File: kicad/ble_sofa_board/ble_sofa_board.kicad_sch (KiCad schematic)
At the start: 4 parts

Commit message: ble_sofa_board - WIP schematic
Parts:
- added D?: 1N5822, Diode_THT:D_DO-201AD_P15.24mm_Horizontal, symbol Diode:1N5822
- added J?: RJ9, symbol Connector:RJ9
- added SW_RST: SW_Push, symbol Switch:SW_Push
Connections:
- net RELAY2_PIN: now reaches A?.10 (GP7)
- net RELAY2_PIN: now also U?.31 (GP7)
- net GND: now reaches A?.13 (GND)
- net GND: now also A?.18 (GND), A?.23 (GND), A?.28 (GND), A?.3 (GND), A?.33 (AGND), A?.38 (GND), A?.8 (GND), U?.13 (GND), U?.18 (GND), U?.23 (GND), U?.28 (GND), U?.3 (GND), U?.33 (AGND), U?.38 (GND), U?.4 (VOUT-), U?.4 (VOUT-), U?.8 (GND), SW_RST.1
- net at A?.30 (RUN): now also U?.11 (RUN), SW_RST.2
- net at A?.35 (ADC_VREF): now also U?.6 (ADC_VREF)
- net at A?.36 (3V3_OUT): now also U?.5 (3V3_OUT)
- net PICO_3V3EN: now reaches A?.37 (3V3_EN)
- net PICO_3V3EN: now also U?.4 (3V3_EN)
- net at A?.39 (VSYS): now also D?.1 (K)
- net RELAY1_PIN: now reaches A?.9 (GP6)
- net RELAY1_PIN: now also U?.32 (GP6)
- net at U?.1 (VBUS): now also U?.2 (VSYS), U?.3 (VOUT+)
- net VCC: now reaches U?.1 (VIN+)
- net VCC: now also U?.1 (VIN+)
- net GND1: now reaches U?.2 (VIN-)
- net GND1: now also U?.2 (VIN-)
- net at U?.3 (VOUT+): now also D?.2 (A)
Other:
- title: (none) -> BLE Sofa Board
- moved on the sheet: A?, U?

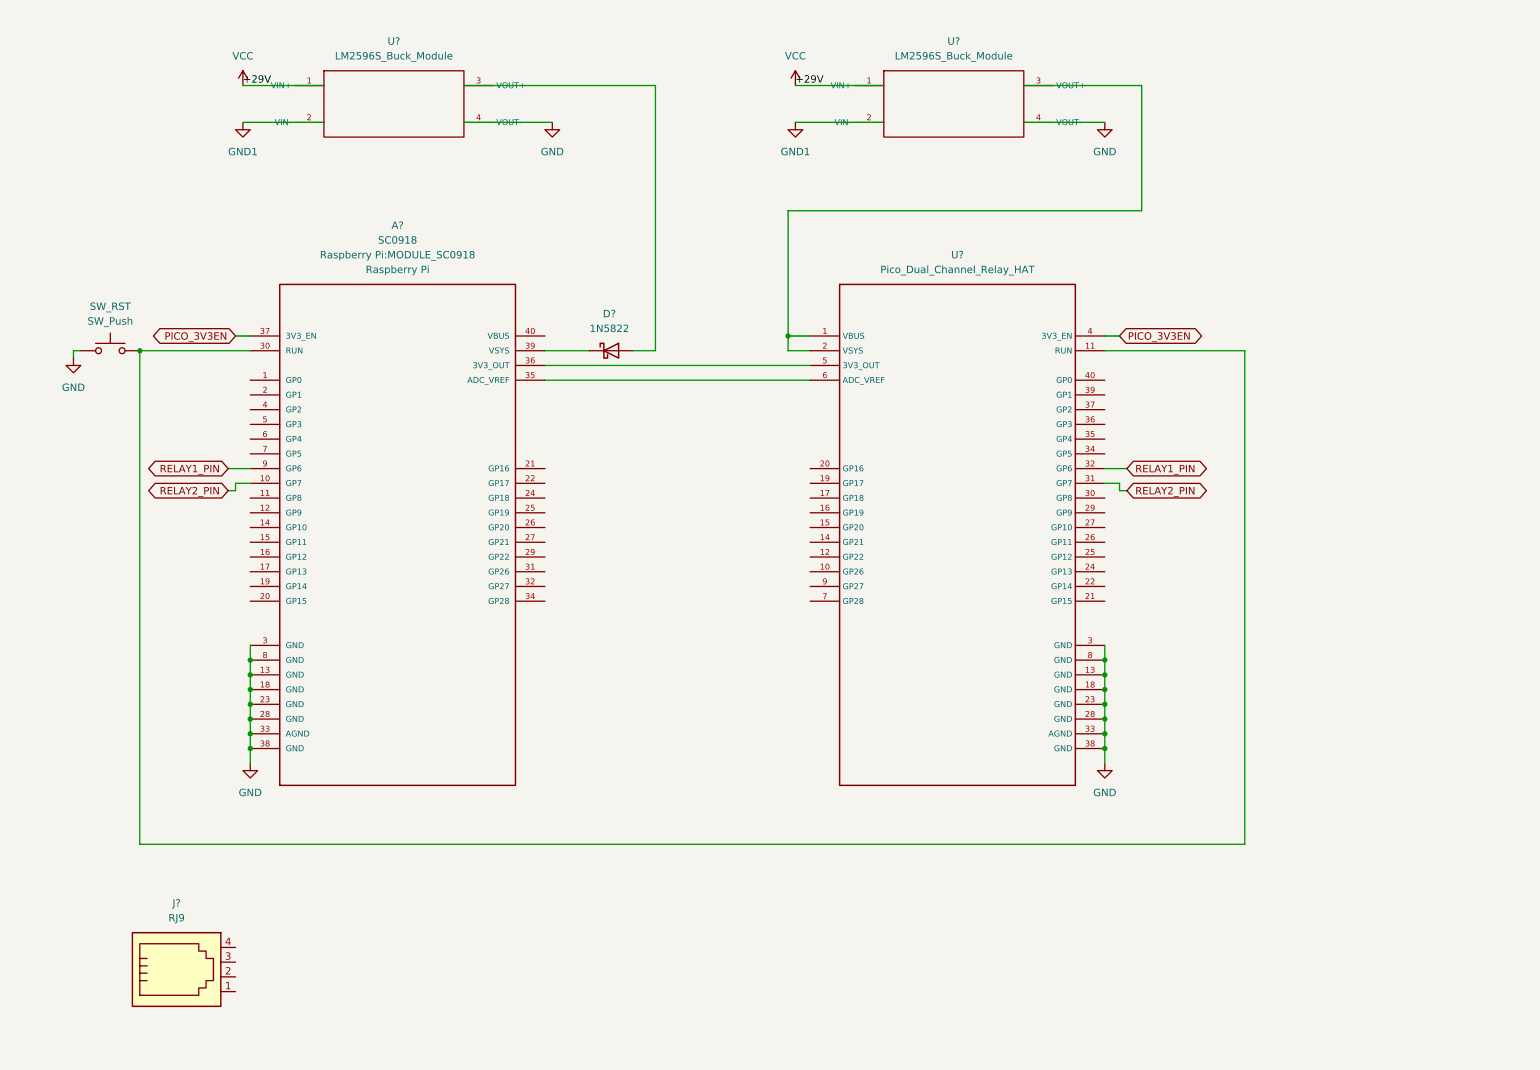
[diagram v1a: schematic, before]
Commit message: ble_sofa_board - Complete schematic and PCB
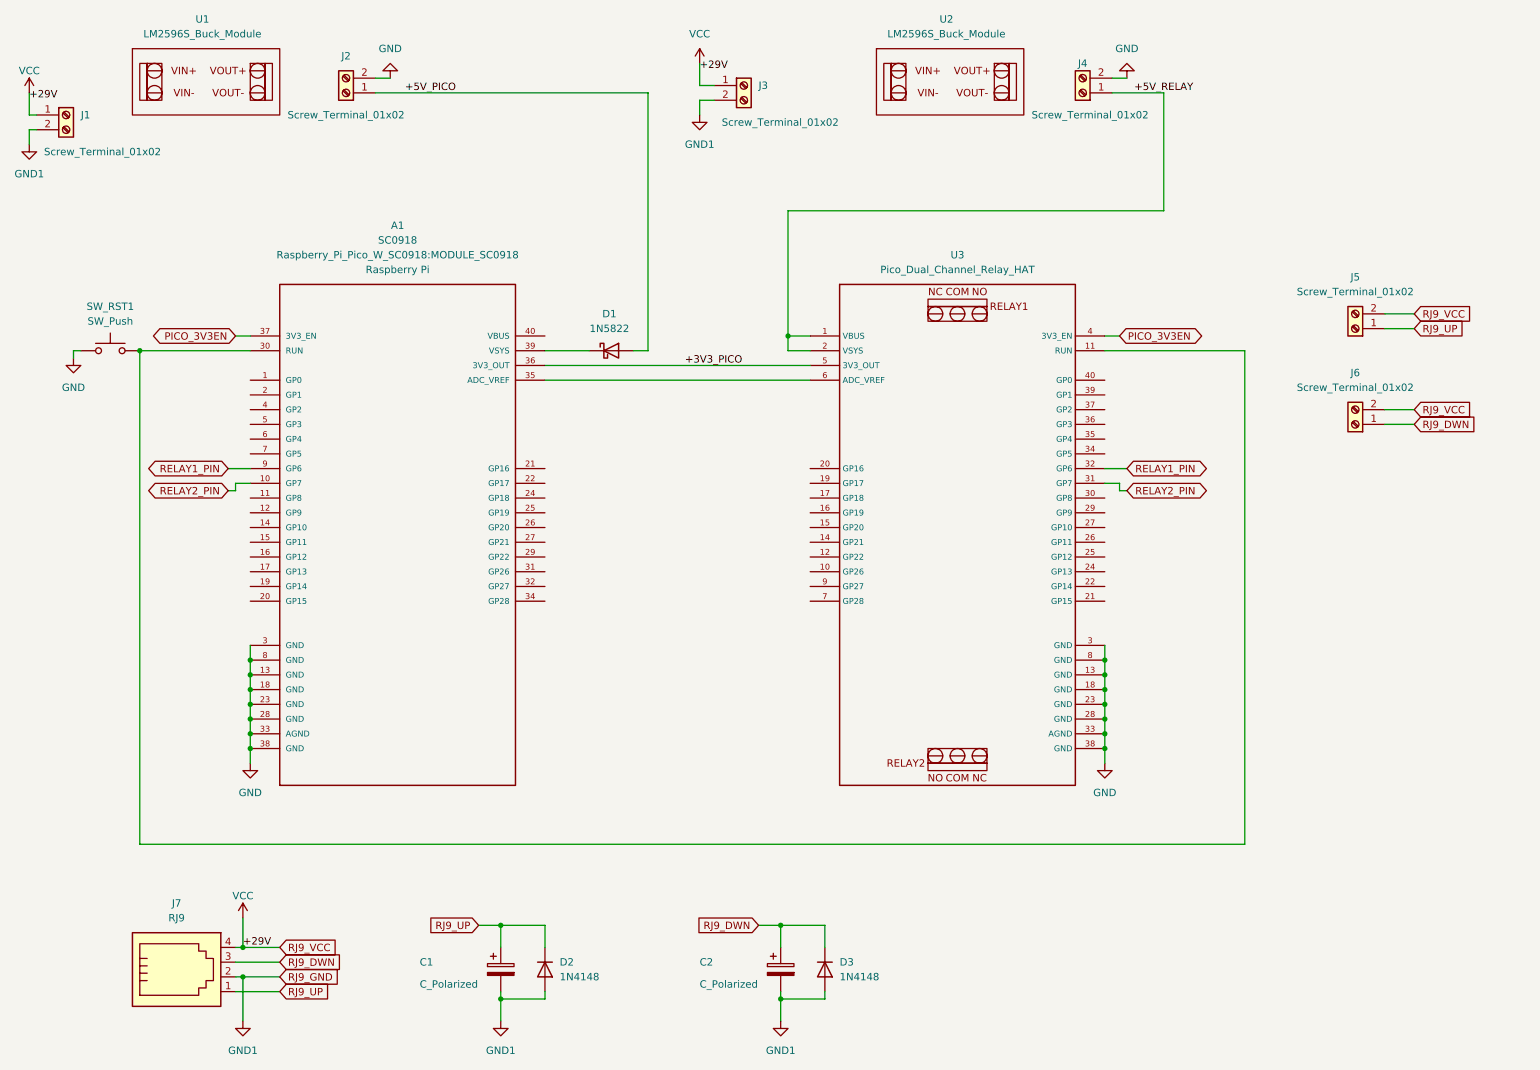
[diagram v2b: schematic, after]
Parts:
- added C1, C2: C_Polarized, Capacitor_THT:CP_Radial_D5.0mm_P2.50mm, symbol Device:C_Polarized
- added D2, D3: 1N4148, Diode_THT:D_DO-35_SOD27_P7.62mm_Horizontal, symbol Diode:1N4148
- added J1, J2, J3, J4, J5, J6: Screw_Terminal_01x02, TerminalBlock:TerminalBlock_bornier-2_P5.08mm, symbol Connector:Screw_Terminal_01x02
- A1: renamed from A?; footprint Raspberry Pi:MODULE_SC0918 -> Raspberry_Pi_Pico_W_SC0918:MODULE_SC0918
- J7: renamed from J?; footprint (none) -> LibreSolar:4P4C_narrow
- SW_RST1: renamed from SW_RST; footprint (none) -> Button_Switch_THT:SW_PUSH_6mm_H4.3mm
- U1, U2: renamed from U?; footprint (none) -> AZ_Delivery:LM2596S_Buck_Module
- U3: renamed from U?; footprint (none) -> SB_Components:Pico_Dual_Channel_Relay_HAT
- gave numbers to parts that had none: 1
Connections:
- net GND: now also J2.2 (Pin_2), J4.2 (Pin_2); no longer U1.4 (VOUT-), U2.4 (VOUT-)
- net GND1: now also J7.2, C1.2, C2.2, D2.2 (A), D3.2 (A), J1.2 (Pin_2), J3.2 (Pin_2); no longer U1.2 (VIN-), U2.2 (VIN-)
- net VCC: now also J7.4, J1.1 (Pin_1), J3.1 (Pin_1), J5.2 (Pin_2), J6.2 (Pin_2); no longer U1.1 (VIN+), U2.1 (VIN+)
- net RJ9_UP: now reaches J7.1
- net RJ9_UP: now also C1.1, D2.1 (K), J5.1 (Pin_1)
- net RJ9_DWN: now reaches J7.3
- net RJ9_DWN: now also C2.1, D3.1 (K), J6.1 (Pin_1)
- net +3V3_PICO: now reaches A1.36 (3V3_OUT), U3.5 (3V3_OUT)
- net +5V_RELAY: now reaches U3.1 (VBUS), U3.2 (VSYS)
- net +5V_RELAY: now also J4.1 (Pin_1); no longer U2.3 (VOUT+)
- net +5V_PICO: now reaches D1.2 (A)
- net +5V_PICO: now also J2.1 (Pin_1); no longer U1.3 (VOUT+)

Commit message: ble_sofa_app - Update schematic
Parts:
- removed J3, J4: Screw_Terminal_01x02, TerminalBlock:TerminalBlock_bornier-2_P5.08mm, symbol Connector:Screw_Terminal_01x02
- removed U2: LM2596S_Buck_Module, AZ_Delivery:LM2596S_Buck_Module, symbol AZ_Delivery:LM2596S_Buck_Module
- added C3, C4: 100nF, symbol Device:C
- added R1: 10K, symbol Device:R
- renumbered D2 to D1, D3 to D2, D1 to D3
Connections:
- net +5V_RELAY is gone; now on an unnamed net: U3.1 (VBUS), U3.2 (VSYS)
- net GND1 is gone; now on net GND: C1.2, C2.2, D1.2 (A), D2.2 (A), J1.2 (Pin_2), J7.2
- net GND: now also C3.2, C4.2
- net RJ9_DWN: now also C4.1
- net RJ9_UP: now also C3.1
- net at A1.30 (RUN), SW_RST1.2: now also R1.2; no longer U3.11 (RUN)
- net at A1.35 (ADC_VREF): no longer U3.6 (ADC_VREF)
- net +3V3_PICO renamed +3V3
- net +3V3: now also R1.1
- net +5V_PICO: no longer names the net of D3.2 (A), J2.1 (Pin_1)
- net PICO_3V3EN: no longer names the net of A1.37 (3V3_EN)
- net PICO_3V3EN: no longer U3.4 (3V3_EN)
- no-connect marks 0 -> 53
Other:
- moved on the sheet: A1, C1, C2, D1, D2, D3, J1, J2, J5, J6, J7, SW_RST1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

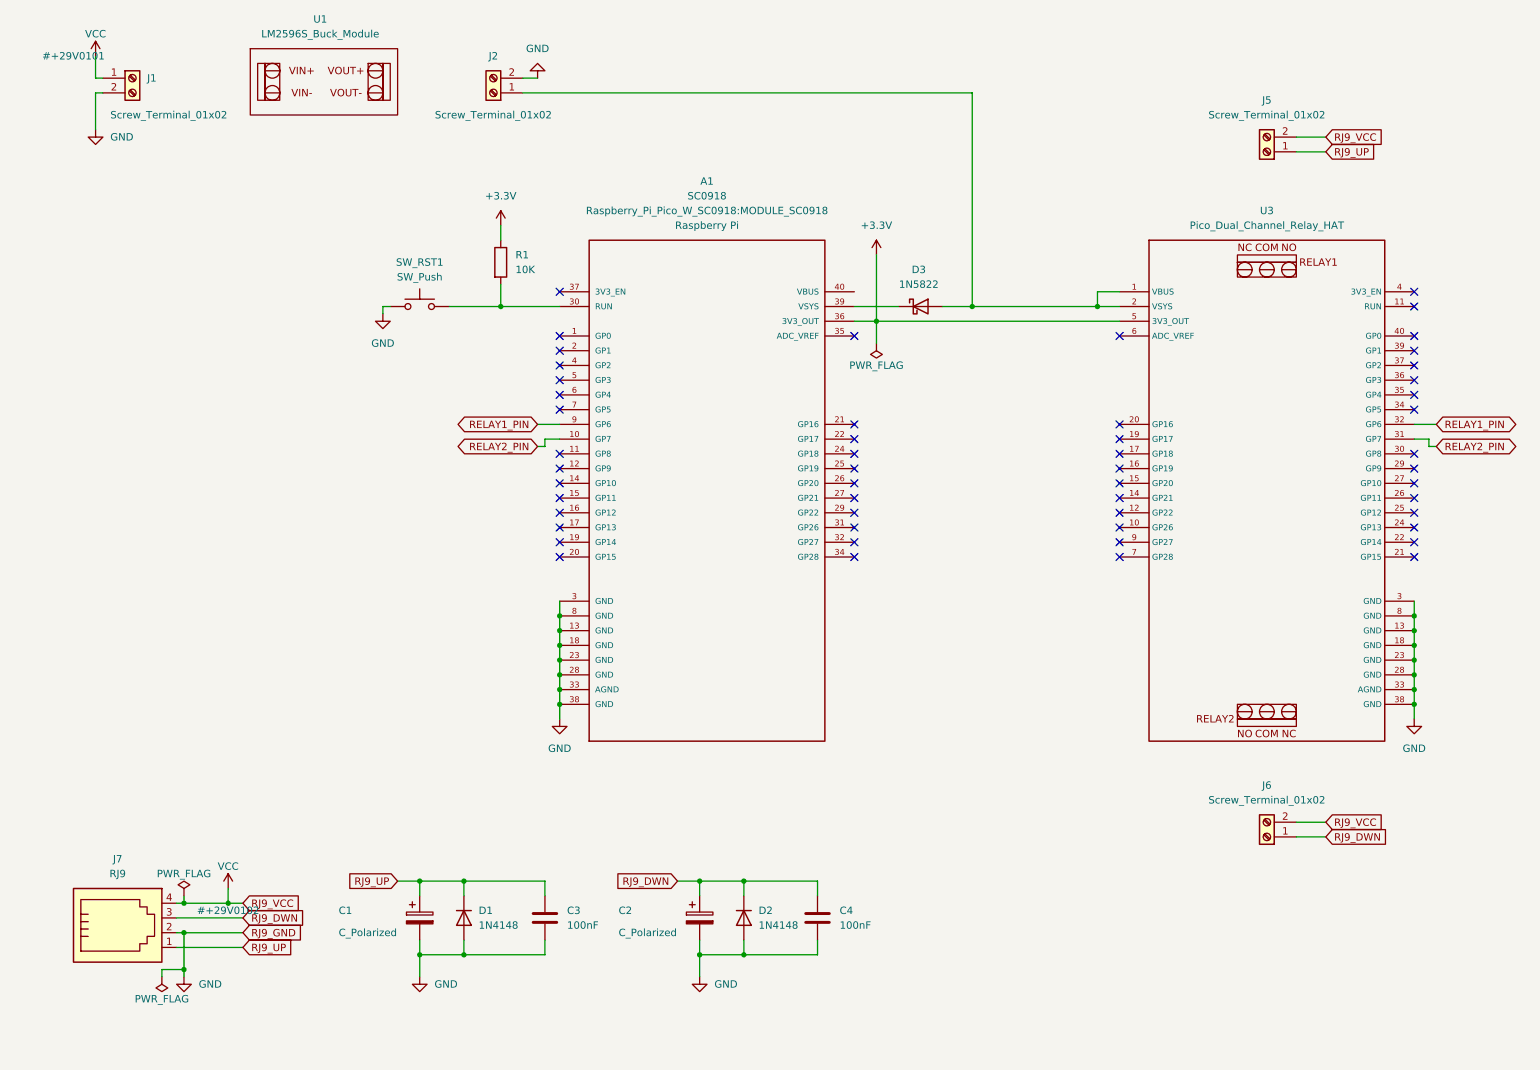
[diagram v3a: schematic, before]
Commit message: ble_sofa_app - Fix ERC in schematic
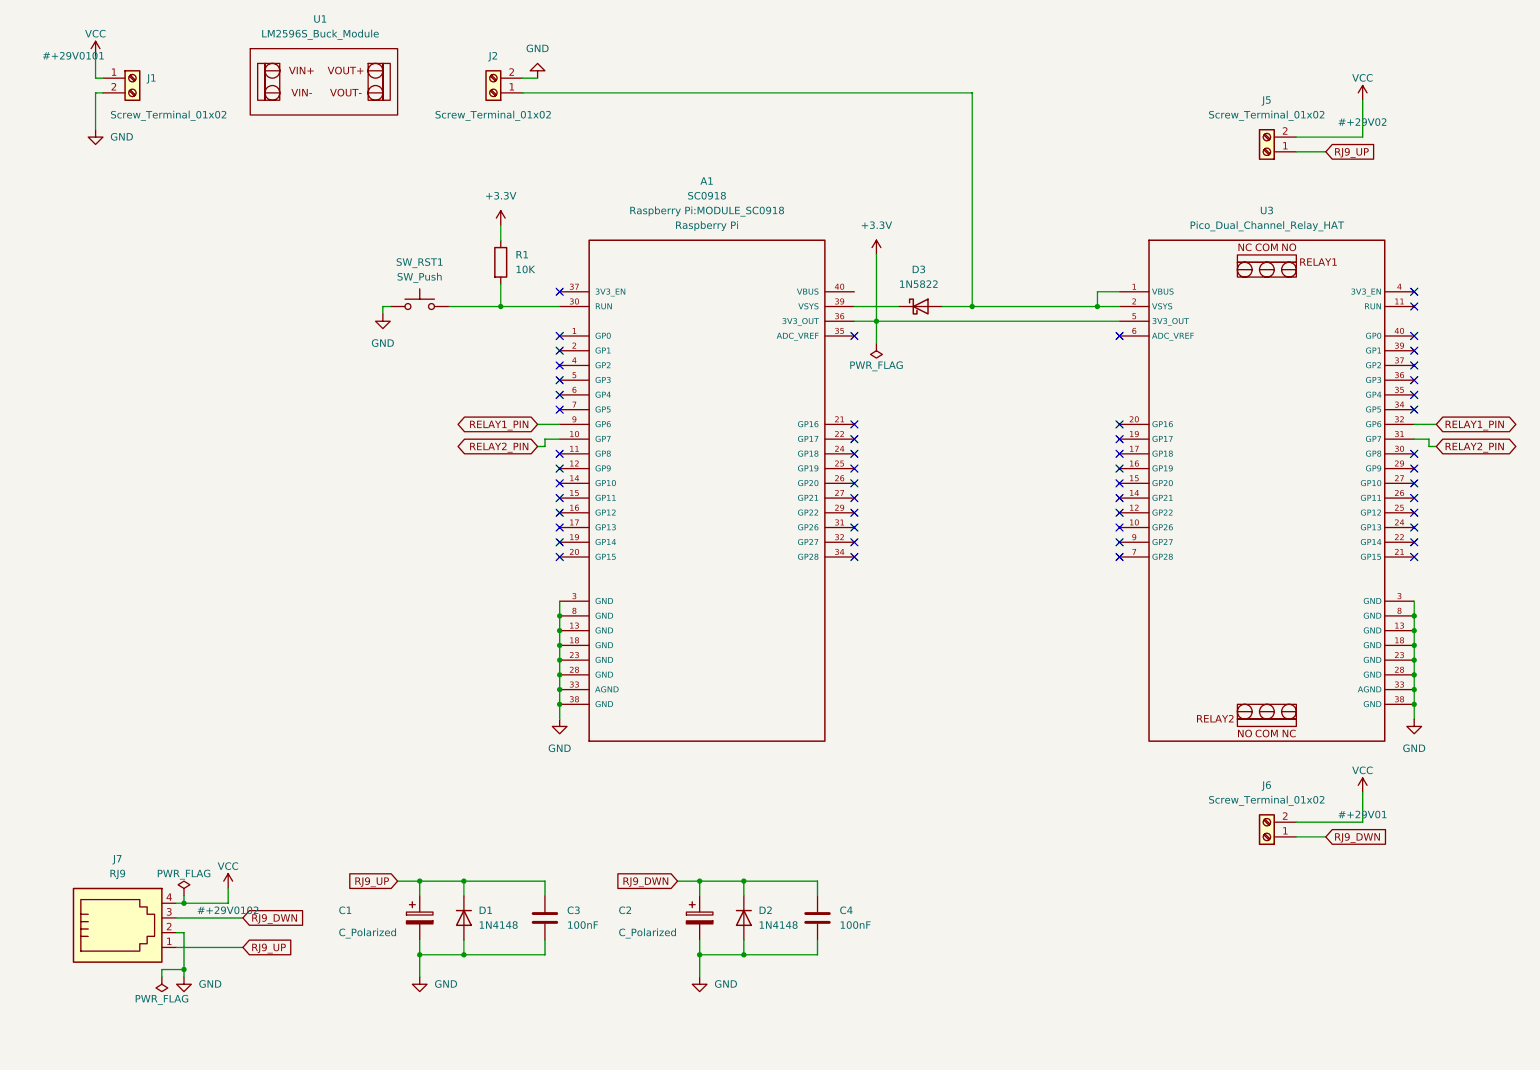
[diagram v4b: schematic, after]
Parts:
- A1: footprint Raspberry_Pi_Pico_W_SC0918:MODULE_SC0918 -> Raspberry Pi:MODULE_SC0918
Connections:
- net +3V3 renamed +3.3V
